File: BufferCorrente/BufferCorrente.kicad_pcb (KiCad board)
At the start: 2 copper layers, 121.5 x 62.5 mm, 41 parts, among them J1 INPUT, J2 OUTPUT, Q1 BD138, Q2 BD138, Q3 BD138, U1 LM318N

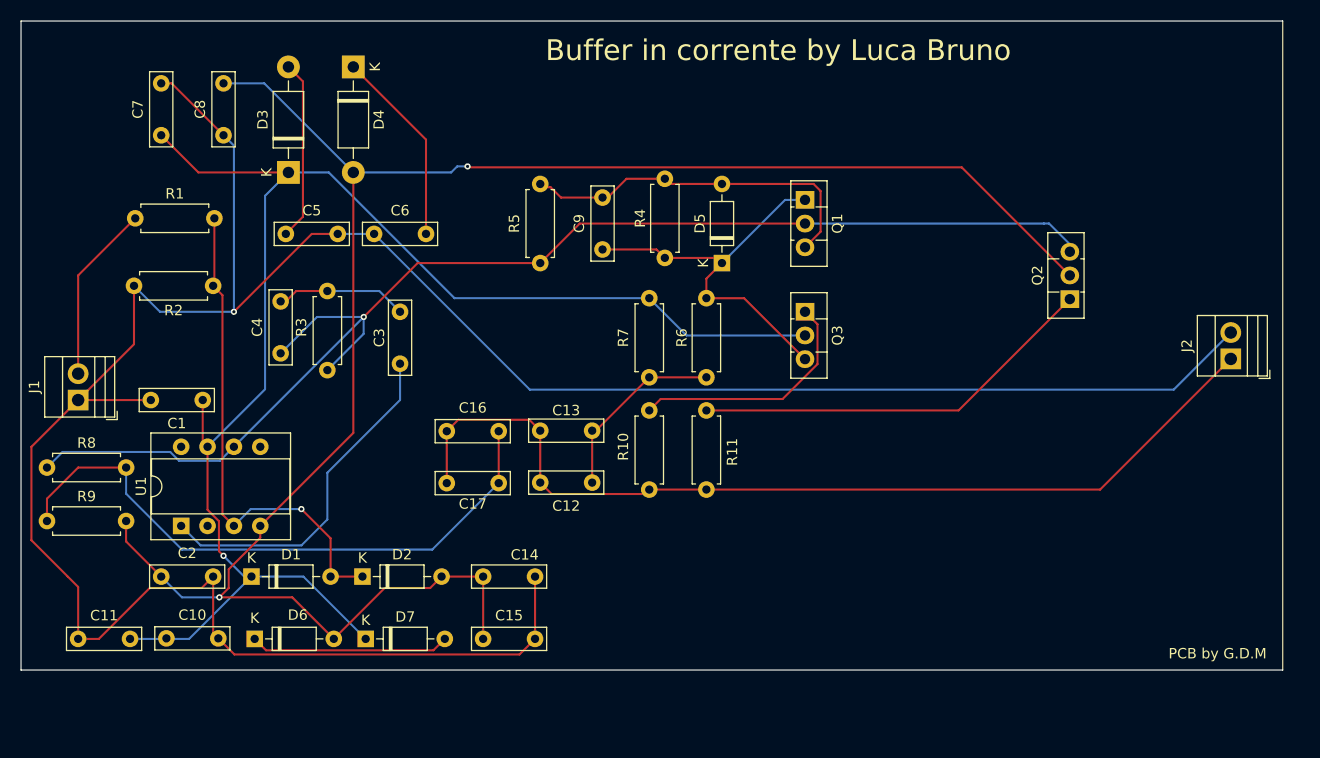
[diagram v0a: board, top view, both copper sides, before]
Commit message: Aggiornata la PCB del buffer in corrente con coponenti SMD e groud plane
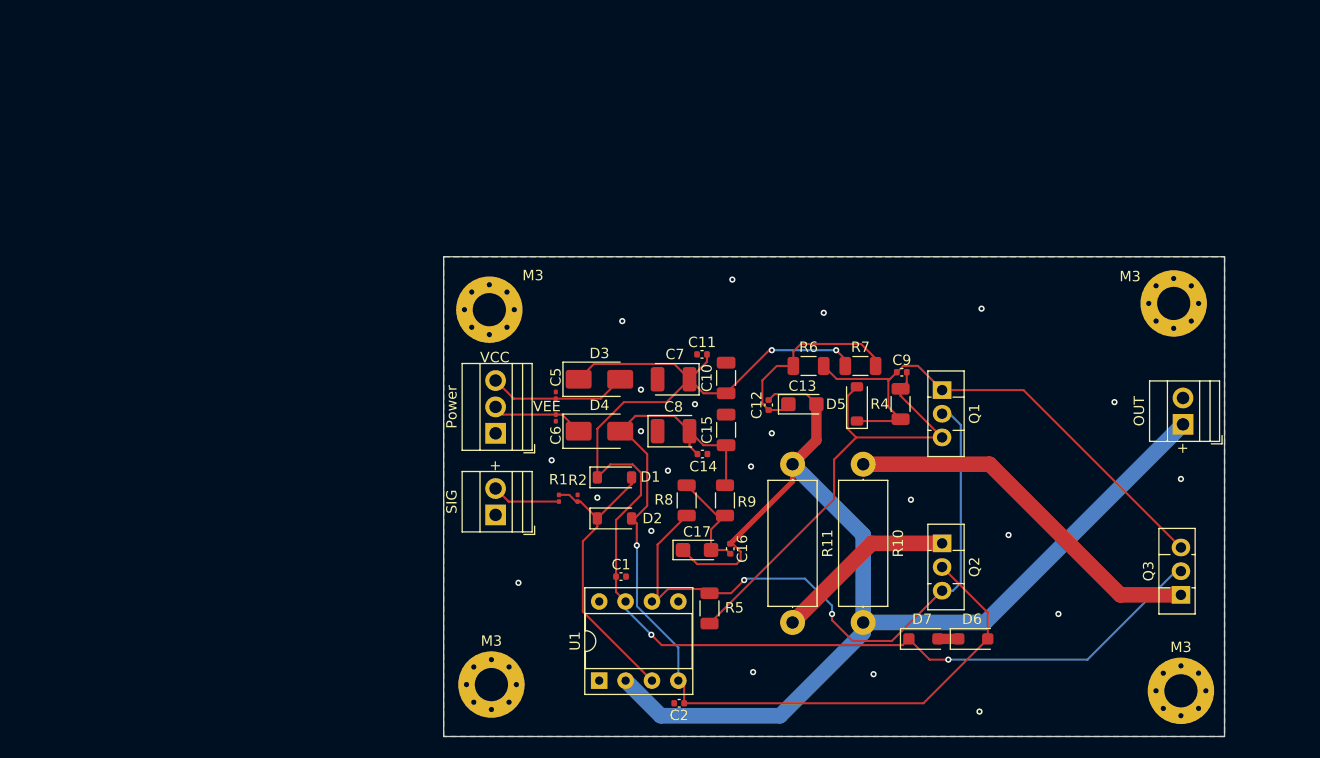
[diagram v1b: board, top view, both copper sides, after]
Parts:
- removed C3, C4: 12pF, Capacitor_THT:C_Rect_L7.0mm_W2.0mm_P5.00mm
- removed J1: INPUT, TerminalBlock:TerminalBlock_Xinya_XY308-2.54-2P_1x02_P2.54mm_Horizontal
- removed J2: OUTPUT, TerminalBlock:TerminalBlock_Xinya_XY308-2.54-2P_1x02_P2.54mm_Horizontal
- removed R3: 10K, Resistor_THT:R_Axial_DIN0207_L6.3mm_D2.5mm_P7.62mm_Horizontal
- added M3: MountingHole_Pad, MountingHole:MountingHole_3.2mm_M3_Pad_Via, F.Cu at (122.8, 117.4)
- added M3: MountingHole_Pad, MountingHole:MountingHole_3.2mm_M3_Pad_Via, F.Cu at (189.2, 118.0)
- added M3: MountingHole_Pad, MountingHole:MountingHole_3.2mm_M3_Pad_Via, F.Cu at (188.5, 80.7)
- added M3: MountingHole_Pad, MountingHole:MountingHole_3.2mm_M3_Pad_Via, F.Cu at (122.6, 81.3)
- added OUT: OUTPUT, TerminalBlock:TerminalBlock_Xinya_XY308-2.54-2P_1x02_P2.54mm_Horizontal, F.Cu at (189.4, 92.3)
- added Power: Differenzial, TerminalBlock:TerminalBlock_Xinya_XY308-2.54-3P_1x03_P2.54mm_Horizontal, F.Cu at (123.2, 93.2)
- added SIG: INPUT, TerminalBlock:TerminalBlock_Xinya_XY308-2.54-2P_1x02_P2.54mm_Horizontal, F.Cu at (123.2, 101.1)
- C1, C2: value 100nF -> 10nF; footprint Capacitor_THT:C_Rect_L7.0mm_W2.0mm_P5.00mm -> Capacitor_SMD:C_0402_1005Metric
- C10, C15: footprint Capacitor_THT:C_Rect_L7.0mm_W2.0mm_P5.00mm -> Capacitor_SMD:C_1206_3216Metric
- C11, C12, C14, C16, C9: footprint Capacitor_THT:C_Rect_L7.0mm_W2.0mm_P5.00mm -> Capacitor_SMD:C_0402_1005Metric
- C13, C17: footprint Capacitor_THT:C_Rect_L7.0mm_W2.0mm_P5.00mm -> Capacitor_Tantalum_SMD:CP_EIA-3216-18_Kemet-A
- C5, C6: footprint Capacitor_THT:C_Rect_L7.0mm_W2.0mm_P5.00mm -> Capacitor_SMD:C_0201_0603Metric
- C7, C8: footprint Capacitor_THT:C_Rect_L7.0mm_W2.0mm_P5.00mm -> Capacitor_Tantalum_SMD:CP_EIA-3528-21_Kemet-B
- D1, D2, D5: footprint Diode_THT:D_DO-35_SOD27_P7.62mm_Horizontal -> Diode_SMD:D_SOD-123
- D3, D4: footprint Diode_THT:D_DO-41_SOD81_P10.16mm_Horizontal -> Diode_SMD:D_SMA
- D6, D7: footprint Diode_THT:D_DO-35_SOD27_P7.62mm_Horizontal -> Diode_SMD:D_SOD-123F
- R1, R2: footprint Resistor_THT:R_Axial_DIN0207_L6.3mm_D2.5mm_P7.62mm_Horizontal -> Resistor_SMD:R_0201_0603Metric
- R10, R11: footprint Resistor_THT:R_Axial_DIN0207_L6.3mm_D2.5mm_P7.62mm_Horizontal -> Resistor_THT:R_Axial_DIN0414_L11.9mm_D4.5mm_P15.24mm_Horizontal
- R4, R5, R6, R7, R8, R9: footprint Resistor_THT:R_Axial_DIN0207_L6.3mm_D2.5mm_P7.62mm_Horizontal -> Resistor_SMD:R_1206_3216Metric
- U1: value LM318N -> OPA134; footprint Package_DIP:CERDIP-8_W7.62mm_SideBrazed_Socket -> Package_DIP:DIP-8_W7.62mm_Socket
- moved D6 69.2 mm to (169.2, 113.0)
- moved C11 66.0 mm to (143.1, 85.6)
- moved R9 65.3 mm to (145.3, 99.7), turned to 90 degrees
- moved R8 61.7 mm to (141.6, 99.7), turned to 90 degrees
- moved C10 59.4 mm to (145.4, 87.9), turned to 90 degrees
- moved C7 54.6 mm to (140.3, 88.0), turned to 180 degrees
- moved D7 53.7 mm to (164.4, 113.0)
- moved C8 51.9 mm to (140.3, 93.0), turned to 0 degrees
- moved C2 51.4 mm to (140.9, 119.2), turned to 180 degrees
- moved R1 48.9 mm to (129.3, 99.5), turned to 90 degrees
- moved Q3 45.3 mm to (189.2, 108.8), turned to 90 degrees
- moved R5 44.0 mm to (143.8, 110.1), turned to 90 degrees
- moved C1 43.7 mm to (135.3, 107.0), turned to 0 degrees
- moved U1 42.9 mm to (133.2, 117.0)
- moved D4 42.3 mm to (133.2, 93.0), turned to 0 degrees
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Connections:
- U1 pad 1: Net-(U1-BAL1) -> unconnected-(U1-VOS-Pad1)
- U1 pad 2: unconnected-(U1---Pad2) -> Net-(J2-Pin_1)
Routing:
- net GND: track 251.1 -> 0.00 mm, vias 1 -> 22
- net -16V: track 184.6 -> 89.4 mm, vias 2 -> 1
- net Net-(Q1-C): track 126.5 -> 63.7 mm, vias 1 -> 2
- net Net-(C16-Pad2): track 59.3 -> 10.8 mm
- net Net-(U1-BAL1): track 33.8 -> 0.00 mm
- net Net-(J2-Pin_1): track 92.2 -> 116.0 mm
- net Net-(Q2-E): track 39.4 -> 17.6 mm
- net Net-(D1-A): track 48.4 -> 28.9 mm, vias 1 -> 0
- net +16V: track 146.6 -> 127.9 mm, vias 1 -> 4
- net Net-(D6-K): track 19.2 -> 2.00 mm
- net Net-(D5-K): track 38.5 -> 51.4 mm
- net Net-(C3-Pad2): track 12.7 -> 0.00 mm
- net Net-(Q3-E): track 23.6 -> 35.8 mm
- net Net-(D5-A): track 34.8 -> 46.1 mm
- net Net-(J1-Pin_2): track 17.2 -> 6.62 mm
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- added copper zone on B.Cu, net GND
- added copper zone on F.Cu, net GND
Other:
- board size 121.5 x 62.5 mm -> 75.2 x 46.2 mm
- board text added: "+"
- board text added: "VCC"
- board text added: "VEE"
- board text removed: "Buffer in corrente by Luca Bruno"
- board text removed: "K"
- board text removed: "PCB by G.D.M"
